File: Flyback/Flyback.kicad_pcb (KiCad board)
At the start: 2 copper layers, 18 parts, among them Q1 IRF840, U1 UC3843_DIP8

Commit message: agregados packages de los componentes
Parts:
- added CCS1: 470p, Capacitor_THT:C_Disc_D3.8mm_W2.6mm_P2.50mm, F.Cu at (200.1, 43.5)
- added CIN1: 100u 400V, Capacitor_THT:C_Radial_D18.0mm_H35.5mm_P7.50mm, F.Cu at (152.4, 34.5)
- added CIN1-U1: 100u 50V, Capacitor_THT:C_Radial_D8.0mm_H11.5mm_P3.50mm, F.Cu at (163.4, 54.3)
- added CIN2: 0.1u 400V, Capacitor_THT:C_Axial_L3.8mm_D2.6mm_P10.00mm_Horizontal, F.Cu at (167.5, 34.9)
- added CIN2-U1: 0.1u 50V, Capacitor_THT:C_Disc_D3.8mm_W2.6mm_P2.50mm, F.Cu at (201.5, 39.4)
- added CMASAS1: 4.7n 2000V, Capacitor_THT:C_Disc_D6.0mm_W2.5mm_P5.00mm, F.Cu at (193.3, 39.3)
- added COUT1: 2200u 16V, Capacitor_THT:C_Radial_D12.5mm_H25.0mm_P5.00mm, F.Cu at (150.9, 51.3)
- added COUT2: 0.1u, Capacitor_THT:C_Disc_D3.8mm_W2.6mm_P2.50mm, F.Cu at (179.8, 56.0)
- added CREG1: 10n, Capacitor_THT:C_Disc_D3.8mm_W2.6mm_P2.50mm, F.Cu at (192.6, 51.0)
- added CT1: 1n, Capacitor_THT:C_Disc_D3.8mm_W2.6mm_P2.50mm, F.Cu at (185.5, 56.0)
- added DLED1: LED, LED_THT:LED_D5.0mm, F.Cu at (193.5, 45.1)
- added JGND1: OUT-, Connector:Banana_Jack_1Pin, F.Cu at (184.7, 47.6)
- added JN1: AC, Connector:Banana_Jack_1Pin, F.Cu at (198.8, 31.0)
- added JOUT1: OUT+, Connector:Banana_Jack_1Pin, F.Cu at (185.5, 35.0)
- added JP-I-IN1: Jumper, Connector_PinHeader_2.54mm:PinHeader_1x02_P2.54mm_Vertical, F.Cu at (29.1, 74.5)
- added JP-IC1: Jumper, Connector_PinHeader_2.54mm:PinHeader_1x02_P2.54mm_Vertical, F.Cu at (29.1, 81.7)
- added JP-ID1: Jumper, Connector_PinHeader_2.54mm:PinHeader_1x02_P2.54mm_Vertical, F.Cu at (33.8, 74.5)
- added JP-IDRAIN1: Jumper, Connector_PinHeader_2.54mm:PinHeader_1x02_P2.54mm_Vertical, F.Cu at (38.4, 74.5)
- added JP-IL1: Jumper, Connector_PinHeader_2.54mm:PinHeader_1x02_P2.54mm_Vertical, F.Cu at (43.0, 74.5)
- added JP-ITH1: Jumper, Connector_PinHeader_2.54mm:PinHeader_1x02_P2.54mm_Vertical, F.Cu at (33.8, 81.7)
- added JV1: AC, Connector:Banana_Jack_1Pin, F.Cu at (172.2, 43.2)
- added RCOMP1: 330 1/4W, Resistor_THT:R_Axial_DIN0207_L6.3mm_D2.5mm_P10.16mm_Horizontal, F.Cu at (108.5, 26.6)
- added RCS1: 1k 1/4W, Resistor_THT:R_Axial_DIN0207_L6.3mm_D2.5mm_P10.16mm_Horizontal, F.Cu at (108.5, 30.6)
- added RFB-PDWN1: 10k 1/4W, Resistor_THT:R_Axial_DIN0207_L6.3mm_D2.5mm_P10.16mm_Horizontal, F.Cu at (121.9, 26.6)
- added RFB1: 3.3k 1/4W, Resistor_THT:R_Axial_DIN0207_L6.3mm_D2.5mm_P10.16mm_Horizontal, F.Cu at (167.5, 30.8)
- added RFB2: 1k 1/4W, Resistor_THT:R_Axial_DIN0207_L6.3mm_D2.5mm_P10.16mm_Horizontal, F.Cu at (108.7, 46.2)
- added RG1: 22 1/4W, Resistor_THT:R_Axial_DIN0207_L6.3mm_D2.5mm_P10.16mm_Horizontal, F.Cu at (108.5, 34.7)
- added RPOL-DF2: 220k 1W, Resistor_THT:R_Axial_DIN0207_L6.3mm_D2.5mm_P10.16mm_Horizontal, F.Cu at (121.9, 30.6)
- added RPOL-LED1: 220 1/4W, Resistor_THT:R_Axial_DIN0207_L6.3mm_D2.5mm_P10.16mm_Horizontal, F.Cu at (180.8, 26.8)
- added RPOL-REG1: 100 1/4W, Resistor_THT:R_Axial_DIN0207_L6.3mm_D2.5mm_P10.16mm_Horizontal, F.Cu at (167.5, 26.8)
- added RT1: 18k 1/4W, Resistor_THT:R_Axial_DIN0207_L6.3mm_D2.5mm_P10.16mm_Horizontal, F.Cu at (108.5, 38.8)
- added RVFB1: 10k CERMET, Potentiometer_THT:Potentiometer_Bourns_3266Y_Vertical, F.Cu at (176.6, 52.5)
- added TH1: Thermistor_NTC, Resistor_THT:R_Axial_DIN0207_L6.3mm_D2.5mm_P2.54mm_Vertical, F.Cu at (172.0, 57.6)

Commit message: Listo
Listo para el route
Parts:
- added F1: 250V 1A, Fuse:Fuseholder_Cylinder-5x20mm_Stelvio-Kontek_PTF78_Horizontal_Open, F.Cu at (69.8, 92.7)
- added L1: L Prim, secund y aux, Flyback:Trafo-E30157, F.Cu at (141.0, 64.8)
- DREG1: footprint Package_TO_SOT_THT:TO-92_Inline -> Package_TO_SOT_THT:TO-92L_Wide
- moved JP-ID1 184.7 mm to (207.0, 138.4), turned to 180 degrees
- moved RS-ID1 183.8 mm to (203.2, 144.8), turned to 90 degrees
- moved DOUT1 173.7 mm to (195.6, 72.4), turned to 180 degrees
- moved DOUT2 173.2 mm to (195.6, 63.5), turned to 180 degrees
- moved RS-IC1 153.4 mm to (182.9, 104.1), turned to 180 degrees
- moved DREG1 143.3 mm to (175.3, 114.3)
- moved JP-IC1 141.9 mm to (170.2, 96.5), turned to 270 degrees
- moved JN1 137.8 mm to (68.6, 76.2)
- moved CCS1 137.8 mm to (108.0, 146.1)
- moved JV1 136.3 mm to (69.8, 133.3)
- moved CIN2-U1 136.3 mm to (109.2, 139.7)
- moved UOPTO1 135.5 mm to (154.9, 137.2), turned to 180 degrees
- moved RSENSE1 134.5 mm to (132.1, 119.4), turned to 270 degrees
- moved CT1 124.0 mm to (100.3, 146.1)
- moved DZG1 122.7 mm to (124.5, 128.3), turned to 270 degrees
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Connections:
- JP-ITH1 pad 1: Net-(JP-ITH1-Pad1) -> I-TH+
- JV1 pad 1: I-IN+ -> Net-(F1-Pad2)
- RS-ITH1 pad 1: Net-(JP-ITH1-Pad1) -> I-TH+

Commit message: autoruteado
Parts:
- RFB2: value 1k 1/4W -> 2.7k 1/4W
- RVFB1: value 10k CERMET -> 1k CERMET
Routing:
- net GND: track 0.00 -> 293.7 mm
- net IC-: track 0.00 -> 231.1 mm
- net ID-: track 0.00 -> 186.2 mm
- net Net-(CREG1-Pad2): track 0.00 -> 158.3 mm
- net I-TH-: track 0.00 -> 129.5 mm
- net ID+: track 0.00 -> 88.4 mm
- net /18V: track 0.00 -> 87.1 mm
- net RCOMP: track 0.00 -> 74.9 mm
- net I-IN+: track 0.00 -> 67.4 mm
- net IDRAIN+: track 0.00 -> 57.8 mm
- net 5V: track 0.00 -> 40.8 mm
- net Net-(Q1-Pad3): track 0.00 -> 38.4 mm
- net IL-: track 0.00 -> 32.2 mm
- net Net-(DZG1-Pad1): track 0.00 -> 31.0 mm
- net Net-(DB1-Pad2): track 0.00 -> 28.5 mm
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
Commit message: PCB_v0
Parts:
- added RL1: 68 2W, Flyback:RCarga30mm, F.Cu at (190.6, 116.2)
- CIN2: footprint Capacitor_THT:C_Axial_L3.8mm_D2.6mm_P10.00mm_Horizontal -> Capacitor_THT:C_Axial_L3.8mm_D2.6mm_P12.50mm_Horizontal
- CMASAS1: footprint Capacitor_THT:C_Disc_D6.0mm_W2.5mm_P5.00mm -> Capacitor_THT:C_Rect_L9.0mm_W3.2mm_P7.50mm_MKT
- CREG1: footprint Capacitor_THT:C_Disc_D3.8mm_W2.6mm_P2.50mm -> Capacitor_THT:C_Rect_L7.2mm_W2.5mm_P5.00mm_FKS2_FKP2_MKS2_MKP2
- DB1: footprint Diode_THT:Diode_Bridge_Round_D9.8mm -> Flyback:PuenteDiodos
- DF2: footprint Diode_THT:D_DO-41_SOD81_P10.16mm_Horizontal -> Diode_THT:D_DO-41_SOD81_P12.70mm_Horizontal
- DREG1: footprint Package_TO_SOT_THT:TO-92L_Wide -> Package_TO_SOT_THT:TO-92L_Inline_Wide
- RFB1, RFB2, RPOL-REG1: footprint Resistor_THT:R_Axial_DIN0207_L6.3mm_D2.5mm_P10.16mm_Horizontal -> Resistor_THT:R_Axial_DIN0309_L9.0mm_D3.2mm_P15.24mm_Horizontal
- RG1: value 22 1/4W -> 10 1/4W
- RPOL-DF2: footprint Resistor_THT:R_Axial_DIN0207_L6.3mm_D2.5mm_P10.16mm_Horizontal -> Flyback:R12,5
- RSENSE1: value 3.3 3W -> 0.5 3W
- moved RS-ID1 91.2 mm to (168.6, 60.4), turned to 0 degrees
- moved JP-ID1 90.2 mm to (174.9, 54.1), turned to 90 degrees
- moved JP-ITH1 74.4 mm to (87.0, 52.7)
- moved RS-ITH1 62.0 mm to (80.6, 57.5)
- moved RPOL-DF2 45.7 mm to (100.5, 67.4), turned to 270 degrees
- moved RVFB1 45.4 mm to (183.1, 101.1), turned to 90 degrees
- moved RPOL-LED1 43.3 mm to (181.9, 143.9), turned to 90 degrees
- moved RS-I-IN1 40.3 mm to (70.7, 123.4), turned to 90 degrees
- moved DLED1 38.6 mm to (174.5, 138.5)
- moved CIN2-U1 35.6 mm to (107.7, 104.1)
- moved CIN1-U1 33.9 mm to (106.7, 96.5), turned to 0 degrees
- moved JP-I-IN1 33.7 mm to (65.7, 117.0), turned to 180 degrees
- moved RFB1 31.7 mm to (169.4, 129.4), turned to 90 degrees
- moved DZG1 31.1 mm to (123.3, 97.2), turned to 90 degrees
- moved CIN1 31.1 mm to (82.8, 85.3), turned to 270 degrees
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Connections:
- DB1 pad 2: Net-(DB1-Pad2) -> I-IN-
- DB1 pad 4: I-IN- -> Net-(DB1-Pad4)
- TH1 pad 1: Net-(DB1-Pad2) -> Net-(DB1-Pad4)
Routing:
- net Net-(CREG1-Pad2): track 158.3 -> 34.0 mm
- net ID-: track 186.2 -> 243.8 mm
- net ID+: track 88.4 -> 32.2 mm
- net I-IN+: track 67.4 -> 32.9 mm
- net /18V: track 87.1 -> 52.9 mm
- net Net-(DB1-Pad2): track 28.5 -> 0.00 mm
- net IC-: track 231.1 -> 255.3 mm
- net Net-(RG1-Pad2): track 28.0 -> 5.80 mm
- net Net-(RPOL-REG1-Pad1): track 14.9 -> 33.6 mm
- net Net-(DB1-Pad4): track 0.00 -> 17.2 mm
- net I-TH-: track 129.5 -> 113.3 mm
- net 5V: track 40.8 -> 25.3 mm
- net RCOMP: track 74.9 -> 59.8 mm
- net Net-(DCL1-Pad2): track 5.08 -> 19.5 mm
- net GND: track 293.7 -> 307.3 mm
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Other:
- net class 0,5 added: clearance 0.5, trace_width 0.5, via_dia 0.8, via_drill 0.4
- net class 2,0 added: clearance 0.5, trace_width 2, via_dia 0.8, via_drill 0.4

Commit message: PCB_v1
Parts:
- moved RVFB1 24.7 mm to (181.0, 125.7), turned to 270 degrees
- moved RCOMP1 6.48 mm to (101.0, 128.6)
- moved RT1 6.48 mm to (90.8, 133.8)
- moved CT1 6.04 mm to (108.6, 132.9)
- moved RPOL-LED1 1.75 mm to (181.0, 142.4)
- moved RS-IC1 1.30 mm to (176.6, 106.2)
- moved JGND1 1.30 mm to (196.4, 136.3)
- moved JP-ID1 1.30 mm to (174.2, 55.2)
- moved CIN1 1.30 mm to (82.1, 86.4)
- moved CIN2-U1 1.30 mm to (107.0, 105.2)
- moved DB1 1.30 mm to (70.0, 99.7)
- moved DF2 1.30 mm to (109.8, 81.4)
- moved TH1 1.30 mm to (70.1, 78.7)
- moved U1 1.30 mm to (102.7, 122.9)
- moved JP-IC1 1.30 mm to (170.2, 111.0)
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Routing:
- net GND: track 307.3 -> 297.0 mm
- net IC-: track 255.3 -> 249.3 mm
- net Net-(CT1-Pad1): track 22.4 -> 18.8 mm
- net Net-(RFB2-Pad2): track 10.8 -> 7.62 mm
- net Net-(DLED1-Pad2): track 8.76 -> 5.96 mm
- net 5V: track 25.3 -> 23.5 mm
- net Net-(CREG1-Pad1): track 14.3 -> 12.5 mm
- net Net-(CREG1-Pad2): track 34.0 -> 32.2 mm
- net RCOMP: track 59.8 -> 58.0 mm
- net ID-: track 243.8 -> 243.1 mm

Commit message: revisado layout 20191013
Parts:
- moved COUT1 20.3 mm to (189.9, 86.9)
- moved CMASAS1 14.1 mm to (139.7, 143.5)
- moved RS-IC1 13.9 mm to (184.9, 95.1), turned to 270 degrees
- moved JP-IC1 13.8 mm to (180.1, 101.4), turned to 0 degrees
- moved COUT2 12.1 mm to (177.7, 84.2), turned to 180 degrees
- moved RL1 6.87 mm to (196.6, 116.0)
- moved CREG1 5.00 mm to (165.1, 136.4)
- moved DLED1 5.00 mm to (173.8, 134.6)
- moved DREG1 5.00 mm to (170.1, 130.1)
- moved RFB1 5.00 mm to (168.7, 125.5)
- moved RFB2 5.00 mm to (175.6, 125.5)
- moved RPOL-LED1 5.00 mm to (181.0, 137.4)
- moved RPOL-REG1 5.00 mm to (161.5, 110.2)
- moved RVFB1 5.00 mm to (181.0, 120.7)
- moved UOPTO1 5.00 mm to (147.3, 134.9)
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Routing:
- net ID-: track 243.1 -> 194.5 mm, vias 0 -> 2
- net IC-: track 249.3 -> 232.2 mm
- net IC+: track 22.9 -> 16.1 mm
- net GND: track 297.0 -> 302.8 mm
- net ID+: track 32.2 -> 29.9 mm
- net RCOMP: track 58.0 -> 60.1 mm
- net /18V: track 52.9 -> 51.2 mm
- added copper zone on B.Cu, net GND
- added copper zone on B.Cu, net IC-
- added copper zone on B.Cu, net ID-
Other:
- board outline added: 150.1 x 100.1 mm

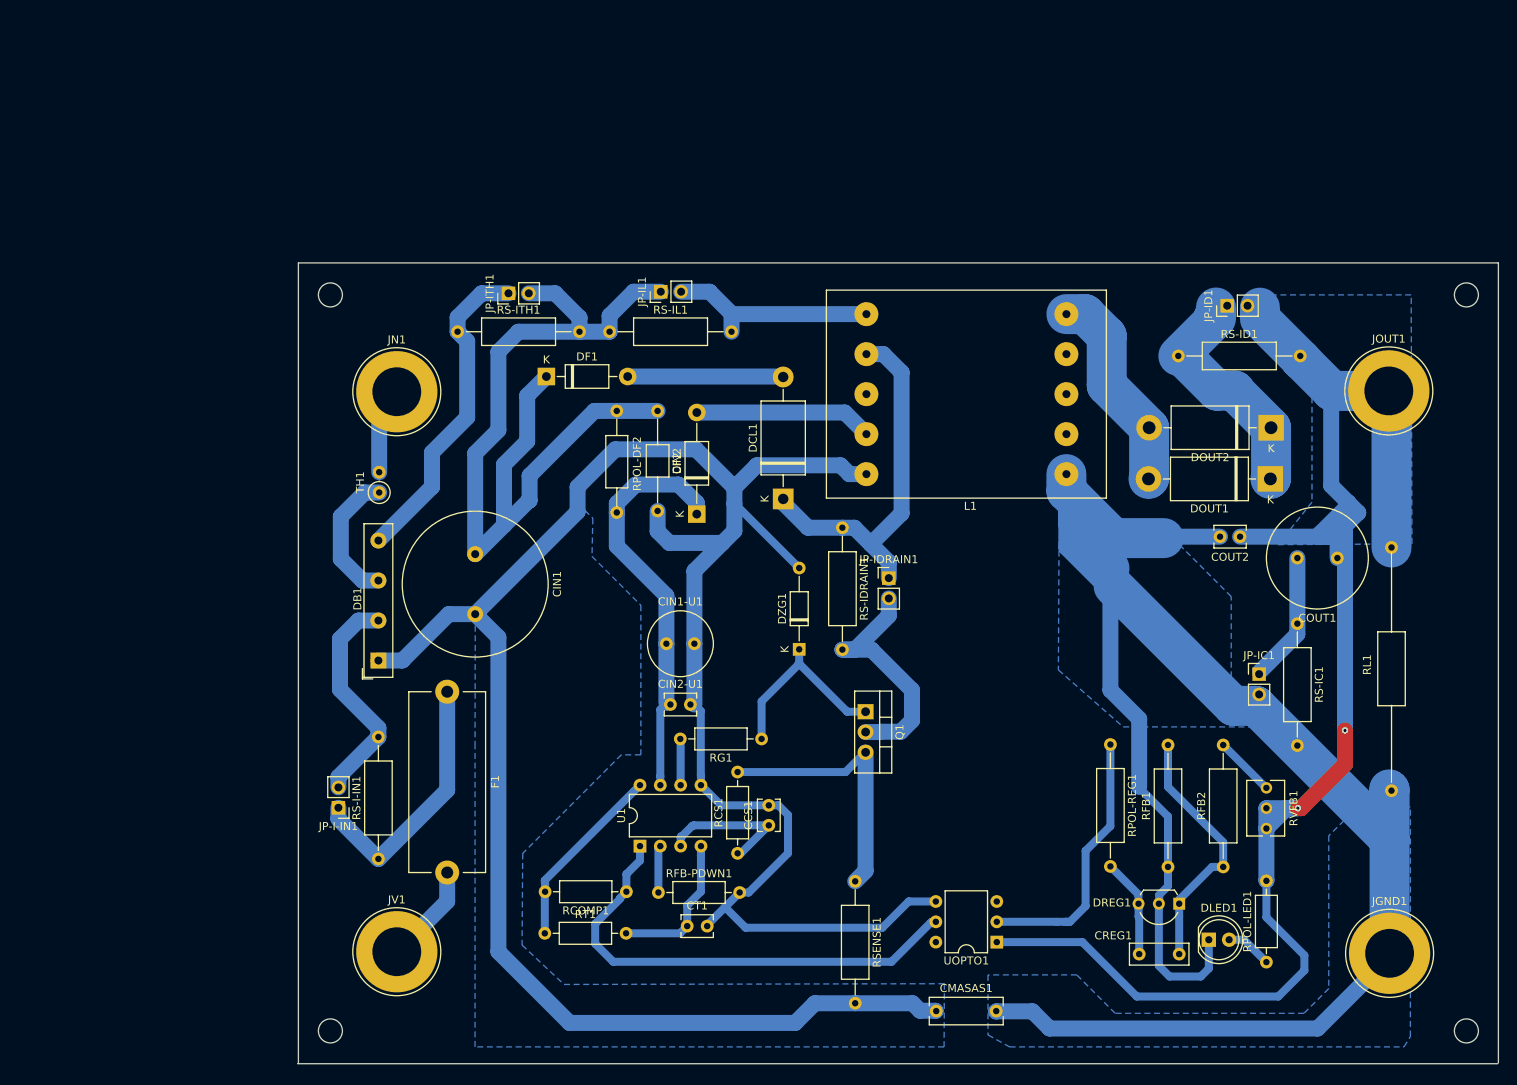
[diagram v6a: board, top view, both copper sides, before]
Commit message: agrandado la Rsense de 3W a 20.32mm de largo y retoques minimos
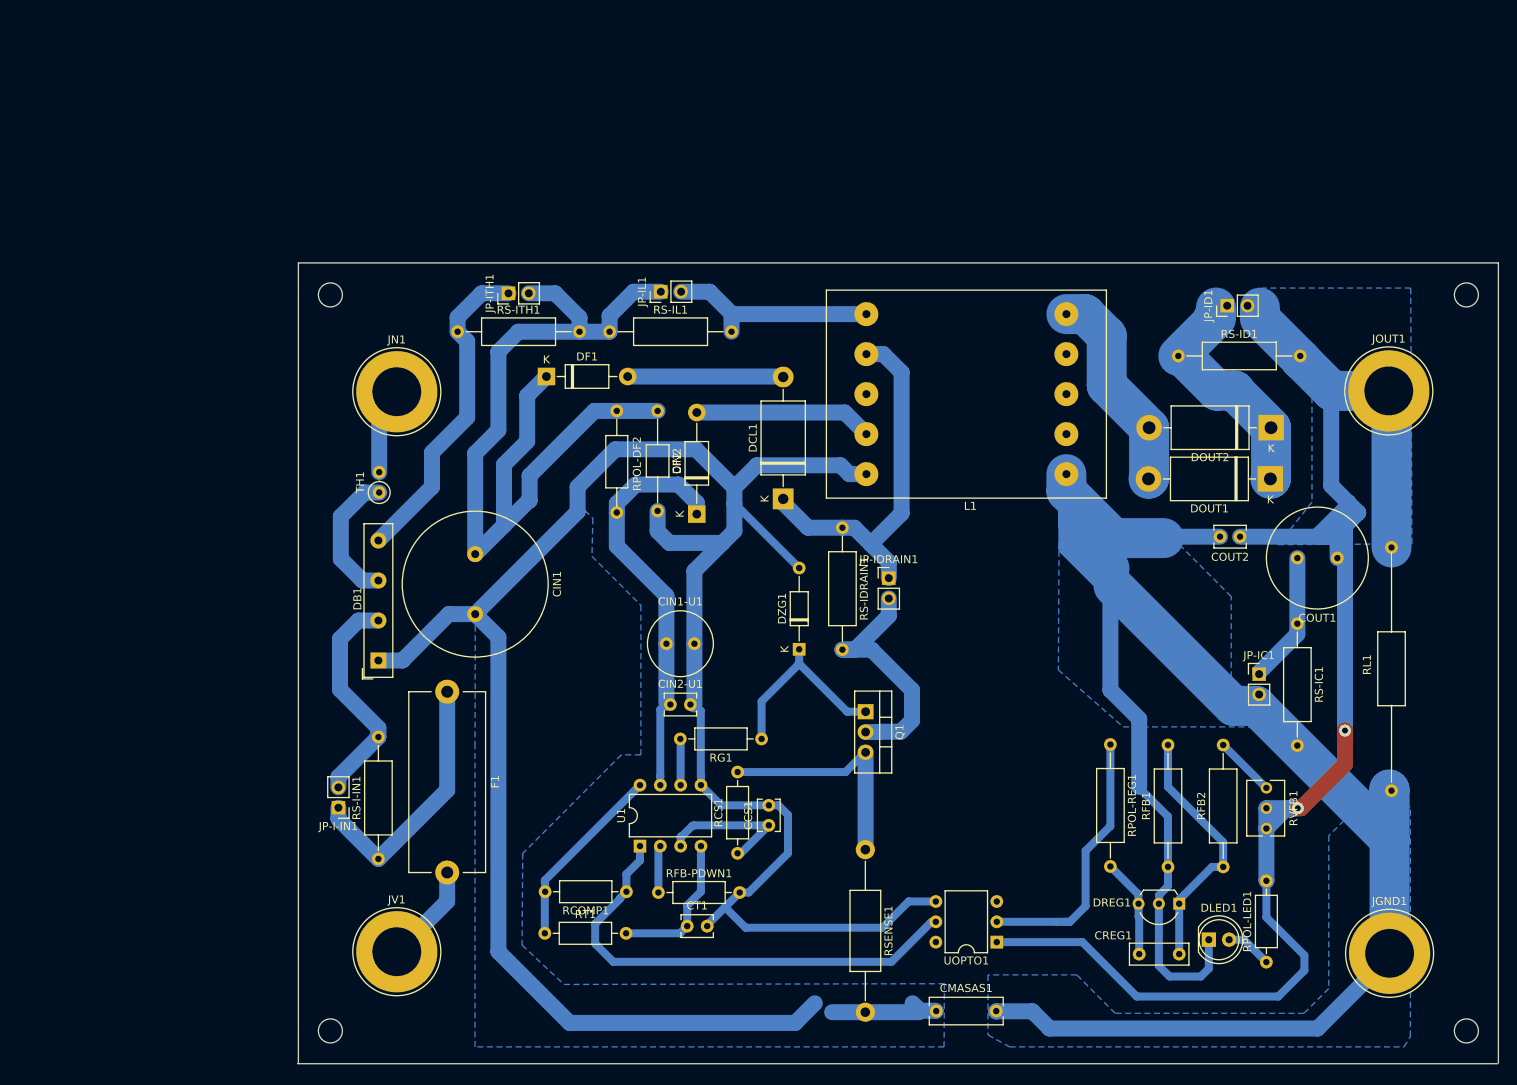
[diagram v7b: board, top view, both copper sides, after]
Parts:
- RSENSE1: footprint Resistor_THT:R_Axial_DIN0309_L9.0mm_D3.2mm_P15.24mm_Horizontal -> Resistor_THT:R_Axial_DIN0411_L9.9mm_D3.6mm_P20.32mm_Horizontal
- moved RSENSE1 4.16 mm to (130.9, 123.3)
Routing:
- net Net-(Q1-Pad3): track 33.7 -> 29.2 mm
- net GND: track 302.8 -> 301.7 mm
